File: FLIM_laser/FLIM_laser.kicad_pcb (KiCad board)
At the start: 2 copper layers, 28.6 x 25 mm, 24 parts, among them J1 Conn_01x02_Male, J2 Conn_01x02_Male, J3 Conn_01x02_Male, J4 Conn_01x02_Male, M1 EP2014C, U1 AMS1117-5.0, U2 LMG1020, U3 74LVC1G08

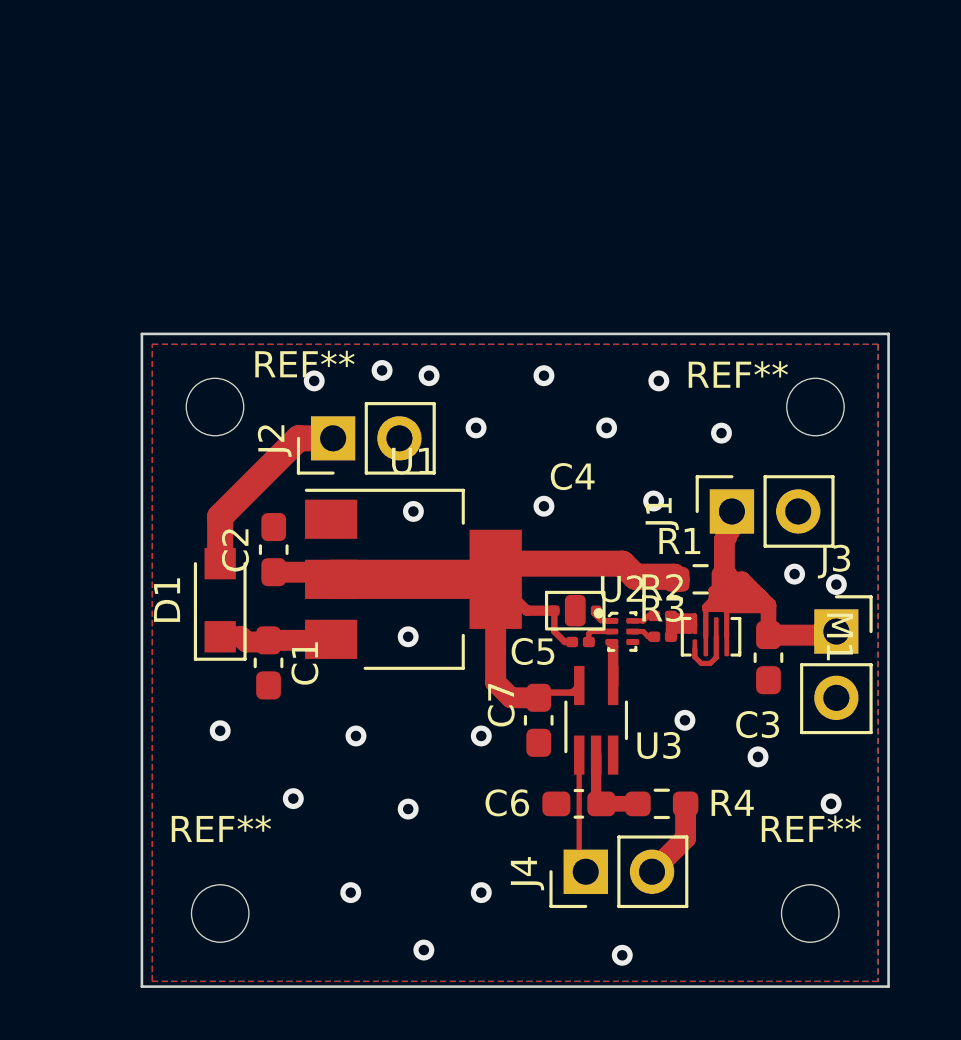
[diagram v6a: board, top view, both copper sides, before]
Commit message: v0.96 Silk was corrected
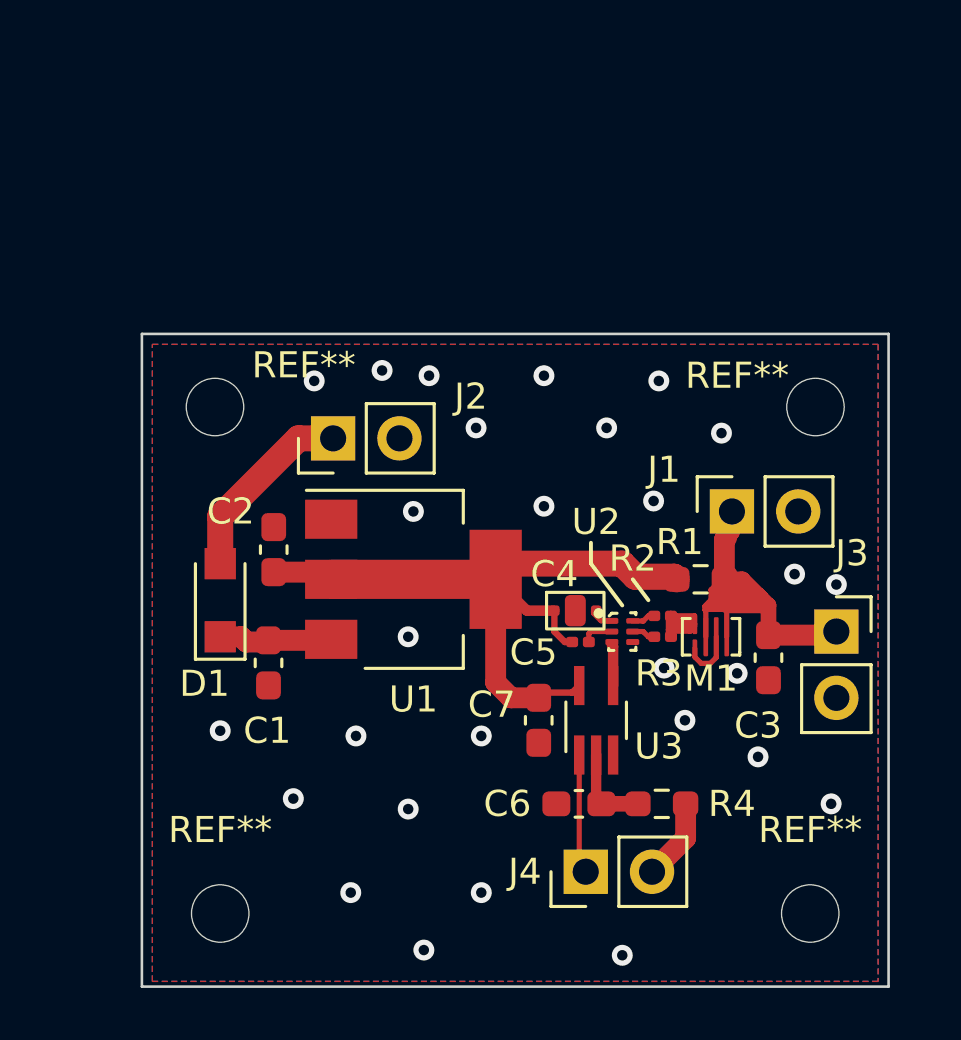
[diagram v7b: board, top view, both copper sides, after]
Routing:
- net GND: vias 26 -> 28
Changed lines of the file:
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@@
     (property "Sheetname" "")
     (attr through_hole)
-    (fp_text reference "J4" (at 0 -2.33 90) (layer "F.SilkS")
+    (fp_text reference "J4" (at 0 -2.33 180) (layer "F.SilkS")
       (effects (font (size 1 1) (thickness 0.15)))
     )
@@
     (property "Sheetname" "")
     (attr smd)
-    (fp_text reference "U1" (at 0 -4.5) (layer "F.SilkS")
+    (fp_text reference "U1" (at 0 4.6) (layer "F.SilkS")
       (effects (font (size 1 1) (thickness 0.15)))
     )
@@
     (property "Sheetname" "")
     (attr smd)
-    (fp_text reference "C4" (at -0.1 -5.1 unlocked) (layer "F.SilkS")
+    (fp_text reference "C4" (at -0.8 -1.4 unlocked) (layer "F.SilkS")
       (effects (font (size 1 1) (thickness 0.15)))
     )
@@
     (property "Sheetname" "")
     (attr smd)
-    (fp_text reference "C2" (at 0 -1.43 90) (layer "F.SilkS")
+    (fp_text reference "C2" (at 1.4625 -1.65 180) (layer "F.SilkS")
       (effects (font (size 1 1) (thickness 0.15)))
     )
@@
     (property "Sheetname" "")
     (attr through_hole)
-    (fp_text reference "J1" (at 0 -2.77 90) (layer "F.SilkS")
+    (fp_text reference "J1" (at 1.6 -2.6 180) (layer "F.SilkS")
       (effects (font (size 1 1) (thickness 0.15)))
     )
@@
     (property "Sheetname" "")
     (attr through_hole)
-    (fp_text reference "J2" (at 0 -2.33 90) (layer "F.SilkS")
+    (fp_text reference "J2" (at 1.6 5.275 180) (layer "F.SilkS")
       (effects (font (size 1 1) (thickness 0.15)))
     )
@@
     (property "Sheetname" "")
     (attr smd)
-    (fp_text reference "C7" (at -0.6 1.4 -270) (layer "F.SilkS")
+    (fp_text reference "C7" (at -0.6 1.8 -180) (layer "F.SilkS")
       (effects (font (size 1 1) (thickness 0.15)))
     )
@@
     (property "Sheetname" "")
     (attr through_hole)
-    (fp_text reference "J3" (at 0 -2.77) (layer "F.SilkS")
+    (fp_text reference "J3" (at 0.6 -3) (layer "F.SilkS")
       (effects (font (size 1 1) (thickness 0.15)))
     )
@@
     (property "Sheetname" "")
     (attr smd)
-    (fp_text reference "C1" (at 0 -1.43 90) (layer "F.SilkS")
+    (fp_text reference "C1" (at 2.6 0.05 180) (layer "F.SilkS")
       (effects (font (size 1 1) (thickness 0.15)))
     )
@@
     (property "Sheetname" "")
     (attr through_hole)
-    (fp_text reference "U2" (at 0 -1.6) (layer "F.SilkS")
+    (fp_text reference "U2" (at -1 -4.2) (layer "F.SilkS")
       (effects (font (size 1 1) (thickness 0.15)))
     )
@@
     (property "Sheetname" "")
     (attr smd)
-    (fp_text reference "D1" (at 0 -2 90) (layer "F.SilkS")
+    (fp_text reference "D1" (at -3.2 -0.6 180) (layer "F.SilkS")
       (effects (font (size 1 1) (thickness 0.15)))
     )
@@
     (property "Sheetname" "")
     (attr smd)
-    (fp_text reference "R2" (at 0 -1.05) (layer "F.SilkS")
+    (fp_text reference "R2" (at -1.145 -2.2) (layer "F.SilkS")
       (effects (font (size 1 1) (thickness 0.15)))
     )
@@
     (property "Sheetname" "")
     (attr smd)
-    (fp_text reference "R3" (at 0 -1.05) (layer "F.SilkS")
+    (fp_text reference "R3" (at -0.145 1.4) (layer "F.SilkS")
       (effects (font (size 1 1) (thickness 0.15)))
     )
@@
     (property "Sheetname" "")
     (attr smd)
-    (fp_text reference "M1" (at 0 -5.5 -90 unlocked) (layer "F.SilkS")
+    (fp_text reference "M1" (at 1.6 -0.6 unlocked) (layer "F.SilkS")
       (effects (font (size 1 1) (thickness 0.15)))
     )
@@
       (net 10 "Net-(C3-Pad1)") (pinfunction "D") (pintype "passive"))
   )
+  (gr_line (start 162.8 47.4) (end 164 49) (layer "F.SilkS") (width 0.15))
+  (gr_line (start 164.4 48) (end 165 48.8) (layer "F.SilkS") (width 0.15))
+  (gr_line (start 162.8 46.6) (end 162.8 47.4) (layer "F.SilkS") (width 0.15))
   (gr_rect (start 145.6 38.6) (end 174.2 63.6) (layer "Edge.Cuts") (width 0.1) (fill none))
   (segment (start 150.3875 50.4) (end 150.45 50.3375) (width 0.8) (layer "F.Cu") (net 1))
@@
   (via (at 170.6 47.8) (size 0.8) (drill 0.4) (layers "F.Cu" "B.Cu") (free) (net 2))
   (via (at 158.4 42.2) (size 0.8) (drill 0.4) (layers "F.Cu" "B.Cu") (free) (net 2))
+  (via (at 165.6 51.4) (size 0.8) (drill 0.4) (layers "F.Cu" "B.Cu") (free) (net 2))
   (via (at 148.6 53.8) (size 0.8) (drill 0.4) (layers "F.Cu" "B.Cu") (free) (net 2))
   (via (at 166.4 53.4) (size 0.8) (drill 0.4) (layers "F.Cu" "B.Cu") (free) (net 2))
@@
   (via (at 163.4 42.2) (size 0.8) (drill 0.4) (layers "F.Cu" "B.Cu") (free) (net 2))
   (via (at 153.6 60) (size 0.8) (drill 0.4) (layers "F.Cu" "B.Cu") (free) (net 2))
+  (via (at 168.4 51.6) (size 0.8) (drill 0.4) (layers "F.Cu" "B.Cu") (free) (net 2))
   (via (at 165.2 45) (size 0.8) (drill 0.4) (layers "F.Cu" "B.Cu") (free) (net 2))
   (via (at 158.6 54) (size 0.8) (drill 0.4) (layers "F.Cu" "B.Cu") (free) (net 2))
